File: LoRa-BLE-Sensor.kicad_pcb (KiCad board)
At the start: 4 copper layers, 96 x 80 mm, 122 parts, among them J1 SHF-105-01-X-D-SM, J2 Battery_Cell, J3 Conn_01x06_Socket, J4 Screw_Terminal_01x04, J5 Screw_Terminal_01x06, J6 Screw_Terminal_01x06, J7 Conn_01x10_Pin, Q1 DMN67D7L, Q10 SQ2389ES, Q11 DMN62D0UDW-7, Q12 DMN62D0UDW-7, Q13 SQ2389ES, Q2 DMN67D7L, Q3 DMN67D7L, Q4 DMN67D7L, Q5 DMN67D7L, Q6 DMN67D7L, Q7 DMN67D7L, Q8 DMN67D7L, Q9 SQ2389ES, SW1 SW_Push, SW2 SW_Push, SW3 SW_Push, U1 RAK4630, U2 NPM1300-QEAA-R, U3 TLV61046ADBVR, U4 TLV61046ADBVR, U5 TLV61046ADBVR

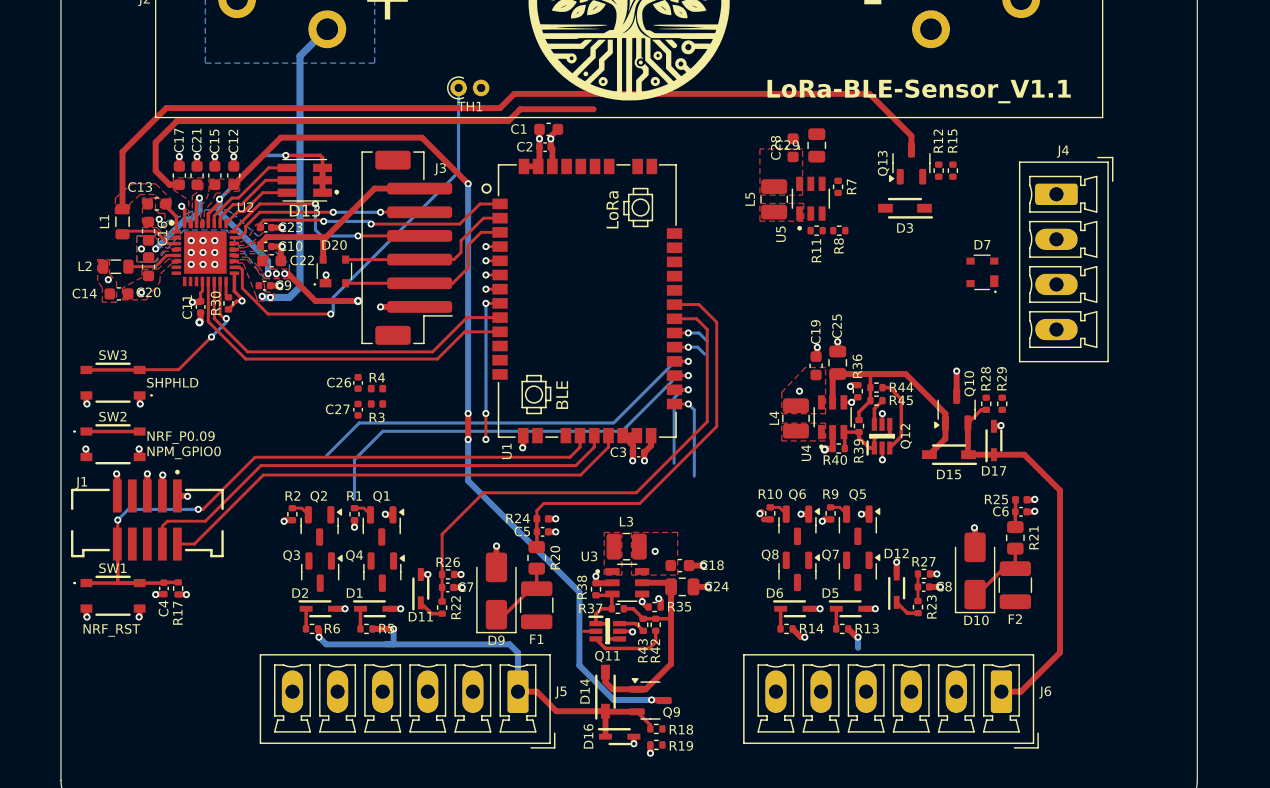
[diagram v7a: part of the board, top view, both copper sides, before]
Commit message: NFC antenna route + connector
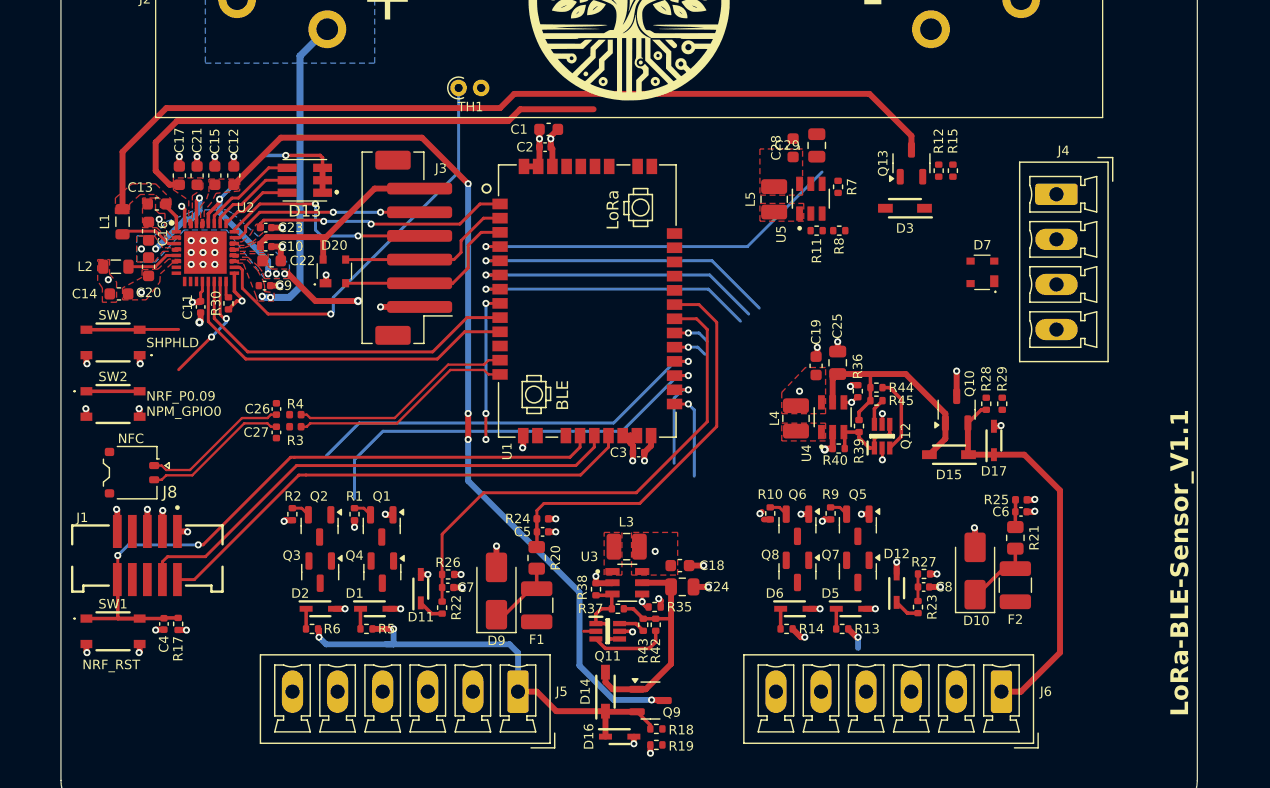
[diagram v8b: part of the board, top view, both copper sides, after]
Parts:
- added J8: Conn_01x02_Socket, User_Connectors:JST_ACH_BM02B-ACHSS-GAN-ETF_1x02-1MP_P1.20mm_Vertical, F.Cu at (70.0, 81.0)
- moved R4 7.24 mm to (83.8, 76.1)
- moved C26 7.24 mm to (82.2, 75.6)
- moved R3 7.16 mm to (83.8, 77.1)
- moved C27 7.16 mm to (82.2, 77.6)
- moved SW3 3.40 mm to (68.4, 70.0)
- moved SW2 3.40 mm to (68.4, 75.2)
- moved C4 3.00 mm to (72.7, 93.8)
- moved J1 3.00 mm to (71.3, 88.0)
- moved R17 3.00 mm to (73.9, 93.8)
- moved SW1 3.00 mm to (68.4, 94.4)
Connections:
- net NFC1 renamed NFC+
- net NFC2 renamed NFC-
- net Net-(C26-Pad1) renamed /NFC_OUT-
- net Net-(C27-Pad1) renamed /NFC_OUT+
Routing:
- net BOOST3_EN: track 1.19 -> 32.2 mm
- net BOOST2_EN: track 2.50 -> 27.3 mm
- net BOOST2_FB_CTRL1: track 2.11 -> 25.7 mm
- net BOOST2_FB_CTRL2: track 2.21 -> 24.8 mm
- net NFC-: track 0.00 -> 19.0 mm
- net NFC+: track 0.00 -> 19.0 mm
- net /NFC_OUT-: track 0.00 -> 12.4 mm
- net /NFC_OUT+: track 0.00 -> 12.4 mm
- net SWDIO: track 40.8 -> 42.0 mm
- net SWCLK: track 41.7 -> 43.0 mm
- net RESET: track 57.6 -> 58.8 mm
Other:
- board text added: "NFC"
